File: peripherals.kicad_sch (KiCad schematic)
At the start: 81 parts, among them J10 533980471, J11 ERF8-040-05.0-L-DV-K-TR, J9 TC2050-IDC-NL, Q10 PJE138K, Q9 PJE138K, U30 TPD4E05U06QDQARQ1, U33 NTS0102GT, U34 PCAL6408ABSHP

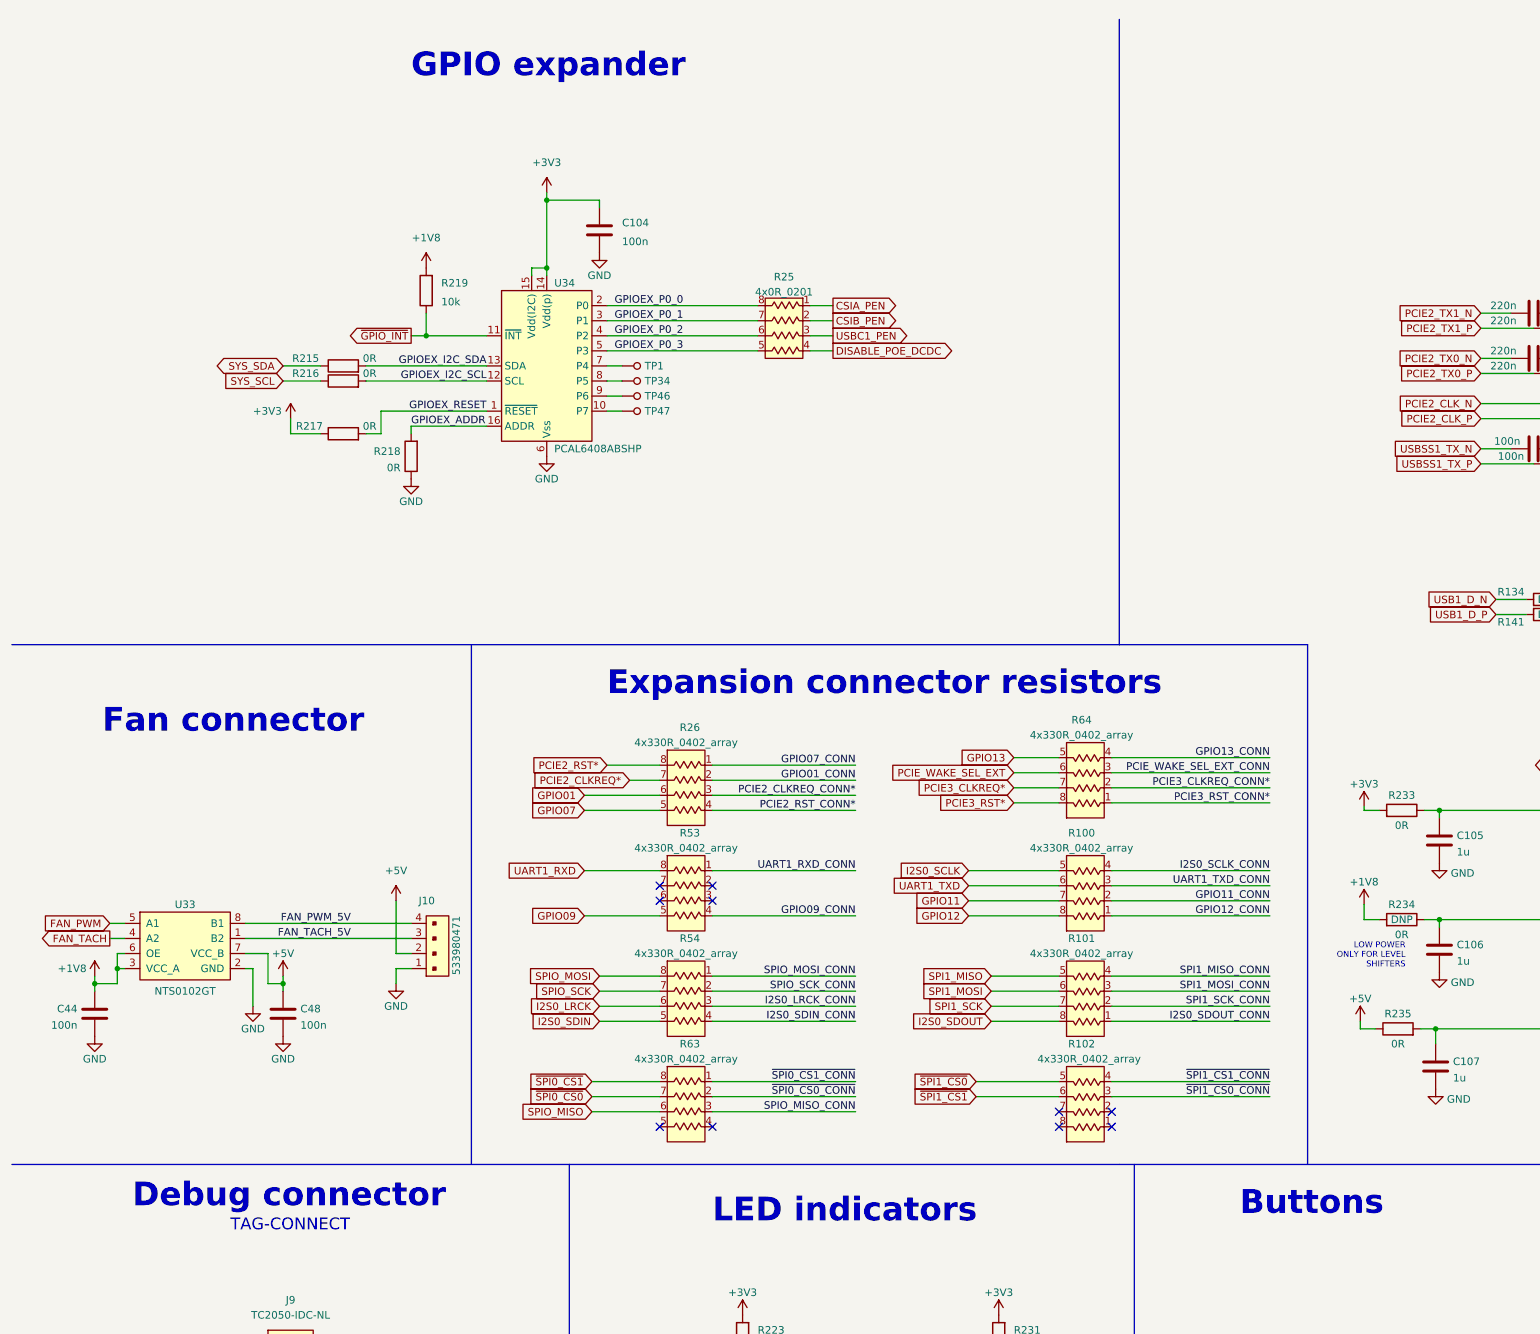
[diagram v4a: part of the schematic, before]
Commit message: Added I2C connector [#40797]
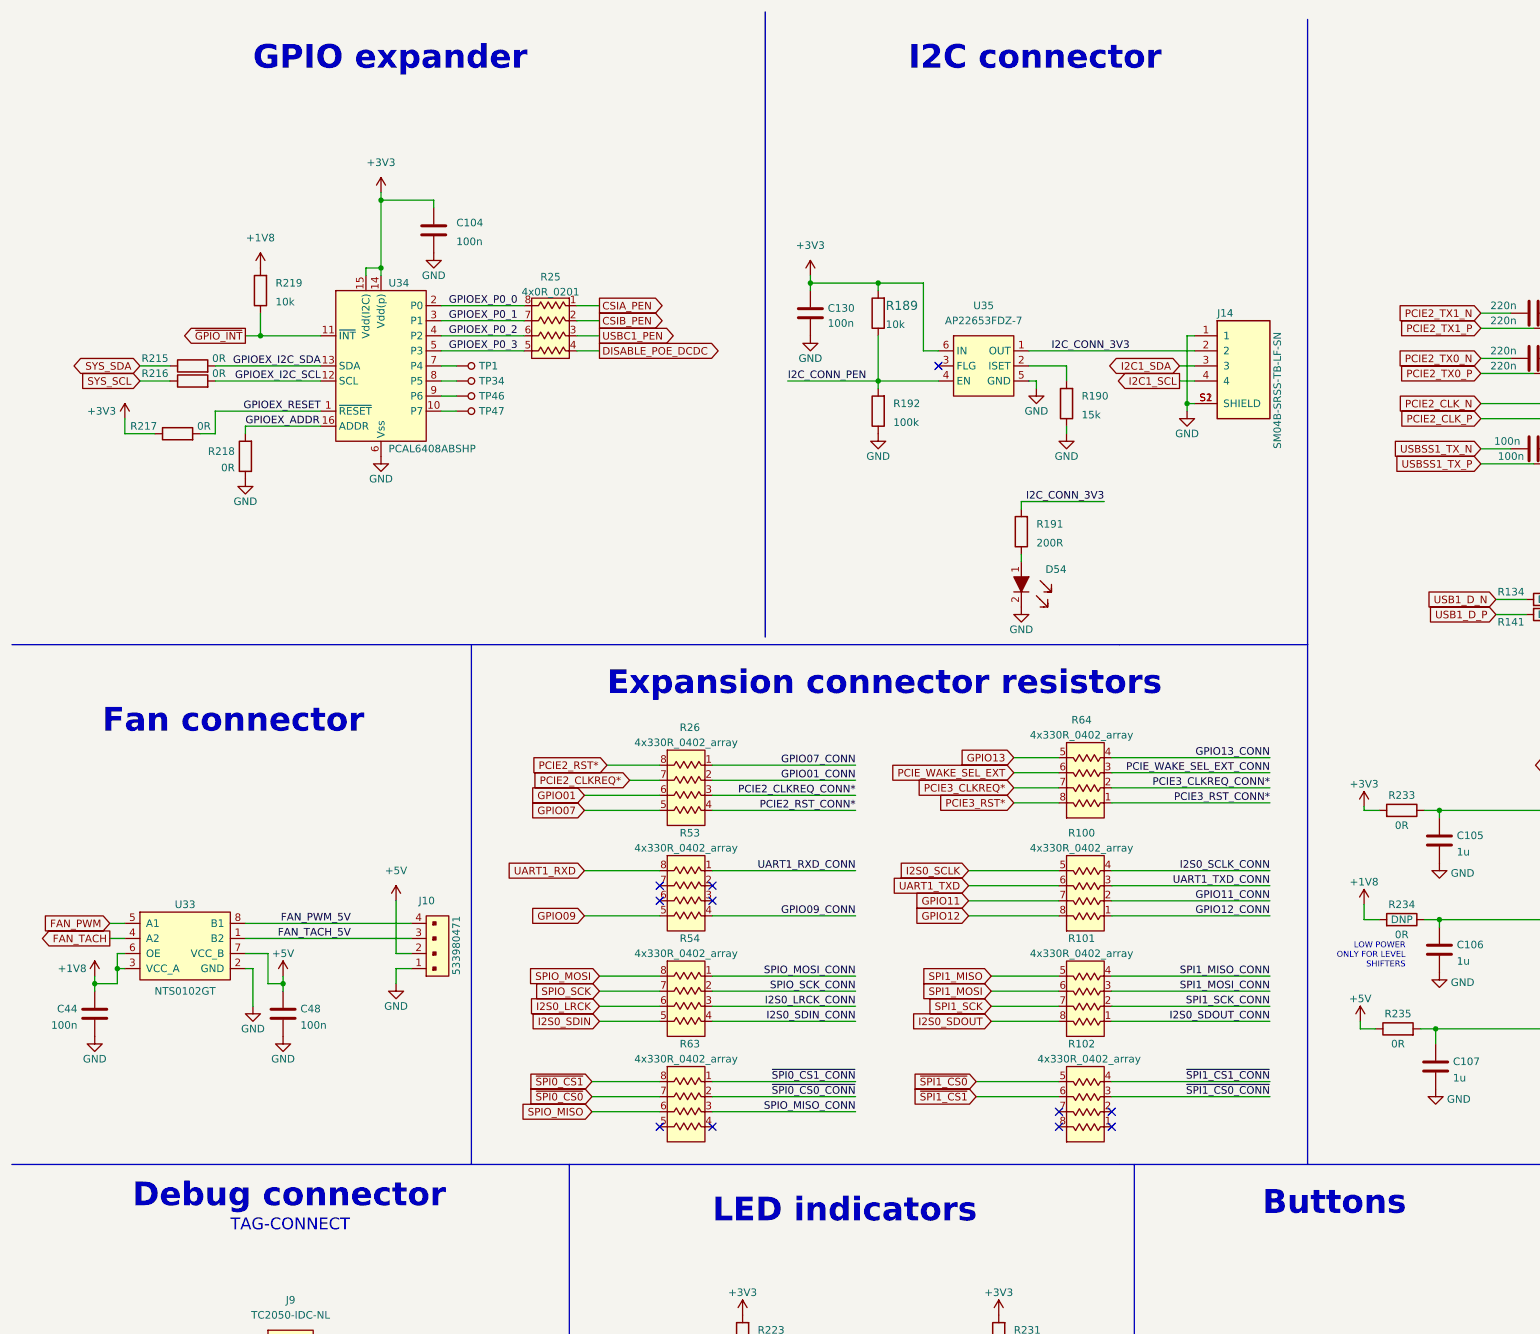
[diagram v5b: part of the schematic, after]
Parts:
- added C130: C_100n_0402, jetson-orin-baseboard-footprints:0402-cap, symbol jetson-orin-baseboard:C_100n_0402
- added D54: LTST-C190GKT, jetson-orin-baseboard-footprints:LED_0603, symbol jetson-orin-baseboard:LTST-C190GKT
- added J14: SM04B-SRSS-TB-LF-SN, antmicro-footprints:SM04B-SRSS-TB-LF-SN, symbol antmicroRectangularConnectorsHeadersMalePins:SM04B-SRSS-TB-LF-SN
- added R189: R_10k_0402, antmicro-footprints:0402-res, symbol antmicroResistors0402:R_10k_0402
- added R190: R_15k_0402, jetson-orin-baseboard-footprints:0402-res, symbol jetson-orin-baseboard:R_15k_0402
- added R191: R_200R_0402, jetson-orin-baseboard-footprints:0402-res, symbol jetson-orin-baseboard:R_200R_0402
- added R192: R_100k_0402, antmicro-footprints:0402-res, symbol antmicroResistors0402:R_100k_0402
- added U35: AP22653FDZ-7, jetson-orin-baseboard-footprints:DFN-6-1EP_2x2mm_P0.65mm_EP1x1.6mm, symbol jetson-orin-baseboard:AP22653FDZ-7
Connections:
- net +3V3: now also C130.1, R189.2, U35.6 (IN)
- net GND: now also C130.2, D54.2, J14.1, J14.S1 (SHIELD), J14.S2 (SHIELD), R190.1, R192.1, U35.5 (GND)
- new net: D54.1, R191.1
- new net: R190.2, U35.2 (ISET)
- new net I2C1_SCL: J14.4
- new net I2C1_SDA: J14.3
- new net I2C_CONN_3V3: J14.2, R191.2, U35.1 (OUT)
- new net I2C_CONN_PEN: R189.1, R192.2, U35.4 (EN)
- no-connect marks 10 -> 11
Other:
- note added: "I2C connector"
- moved on the sheet: C104, R215, R216, R217, R218, R219, R25, TP1, TP34, TP46, TP47, U34

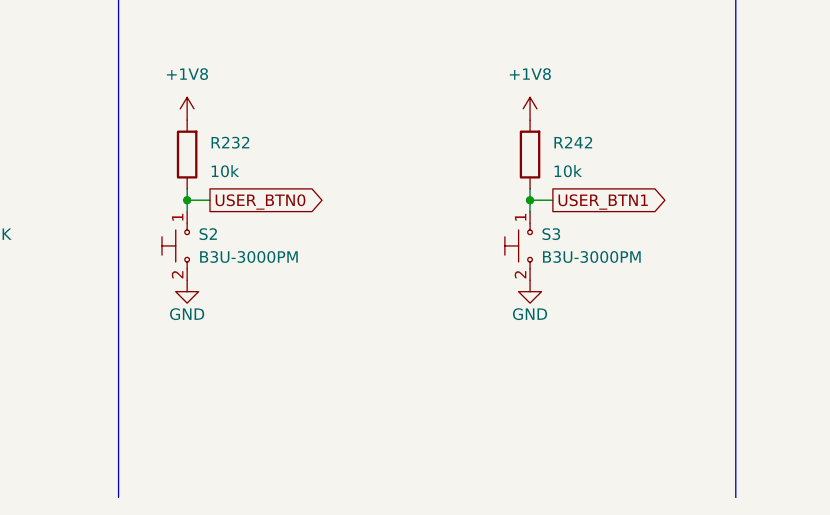
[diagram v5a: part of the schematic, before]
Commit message: Replace buttons with top-actuated ones
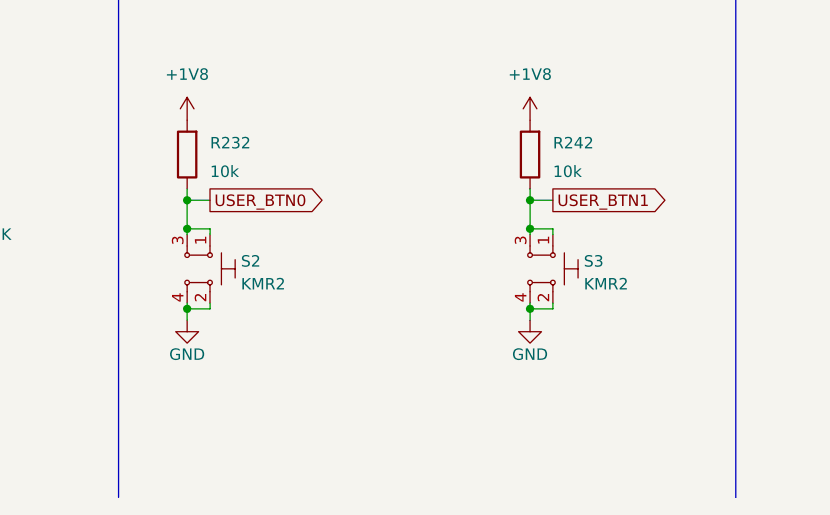
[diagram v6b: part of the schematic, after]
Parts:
- removed S2, S3: B3U-3000PM, jetson-orin-baseboard-footprints:B3U-3000P, symbol jetson-orin-baseboard:B3U-3000PM
- added S2, S3: KMR2, antmicro-footprints:SW_SPST_4.2x2.8, symbol antmicroPushbuttonSwitches:KMR2
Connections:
- net GND: now also S2.2, S2.4, S3.2, S3.4
- net USER_BTN0: now also S2.1, S2.3
- net USER_BTN1: now also S3.1, S3.3

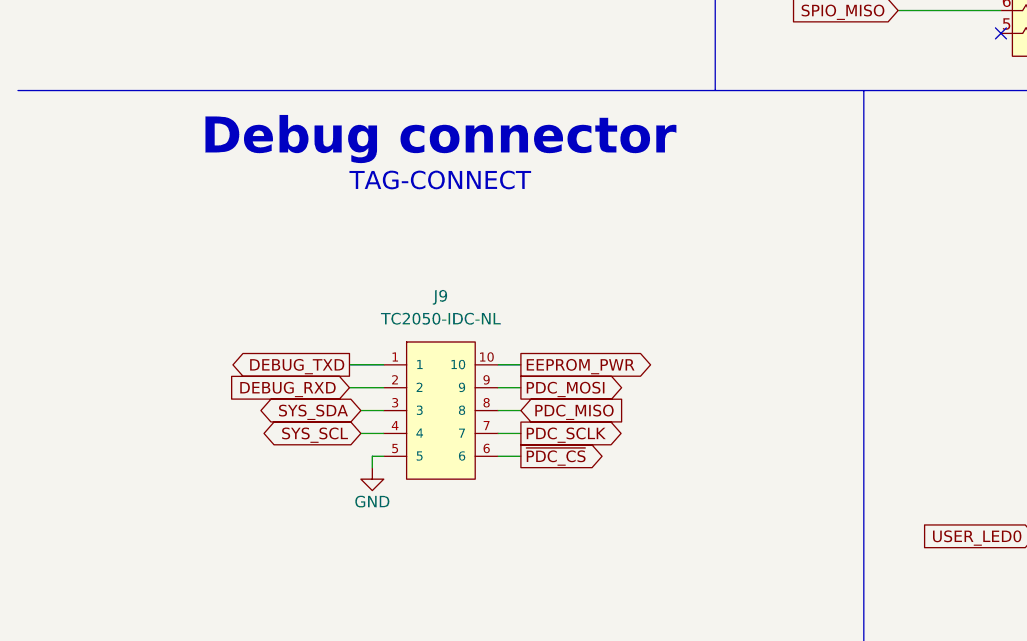
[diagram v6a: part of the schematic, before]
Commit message: Change tag-connect to 2x5 pin 1.27 header
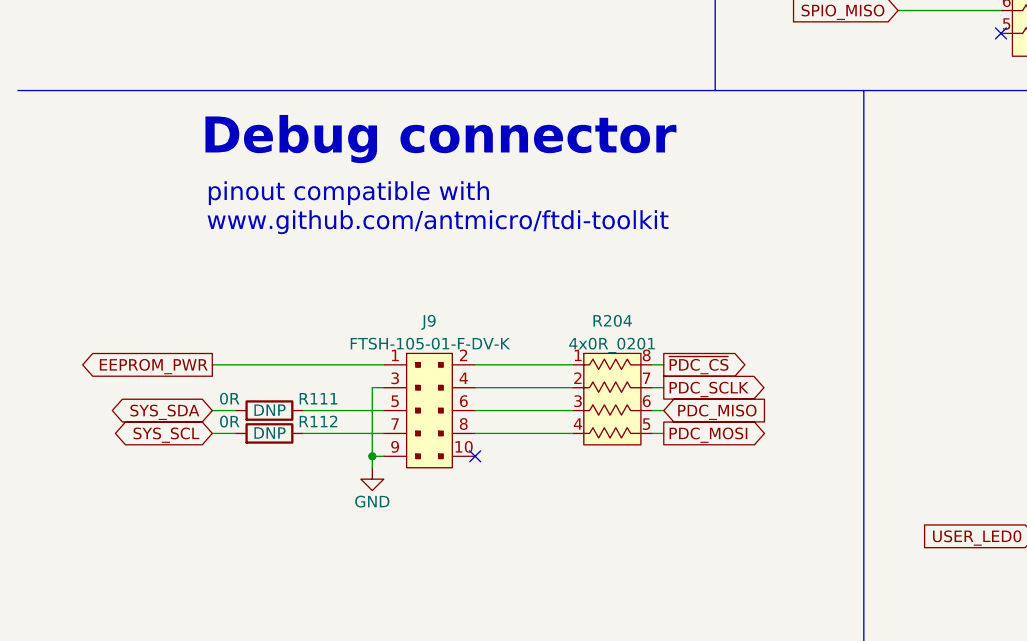
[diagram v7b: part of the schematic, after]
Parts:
- removed J9: TC2050-IDC-NL, jetson-orin-baseboard-footprints:TC2050-IDC-NL_2x05_Vertical, symbol jetson-orin-baseboard:TC2050-IDC-NL
- added J9: FTSH-105-01-F-DV-K, antmicro-footprints:PinHeader_2x5_P1.27_SMD, symbol antmicroRectangularConnectorsHeadersMalePins:FTSH-105-01-F-DV-K
- added R111, R112: R_0R_0402, jetson-orin-baseboard-footprints:0402-res, symbol jetson-orin-baseboard:R_0R_0402
- added R204: 4x0R_0201_array, antmicro-footprints:EXB18V, symbol antmicroResistorNetworksArrays:4x0R_0201_array
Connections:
- net EEPROM_PWR: now also J9.1
- net GND: now also J9.3, J9.9
- net PDC_MISO: now also R204.6
- net PDC_MOSI: now also R204.5
- net PDC_SCLK: now also R204.7
- net SYS_SCL: now also R112.2
- net SYS_SDA: now also R111.2
- net ~{PDC_CS}: now also R204.8
- new net: J9.5, R111.1
- new net: J9.7, R112.1
- new net: J9.2, R204.1
- new net: J9.4, R204.2
- new net: J9.6, R204.3
- new net: J9.8, R204.4
- no-connect marks 11 -> 12
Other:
- note added: "pinout compatible with www.github.com/antmicro/ftdi-toolkit"
- note removed: "TAG-CONNECT"
